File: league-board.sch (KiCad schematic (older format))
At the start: 14 parts

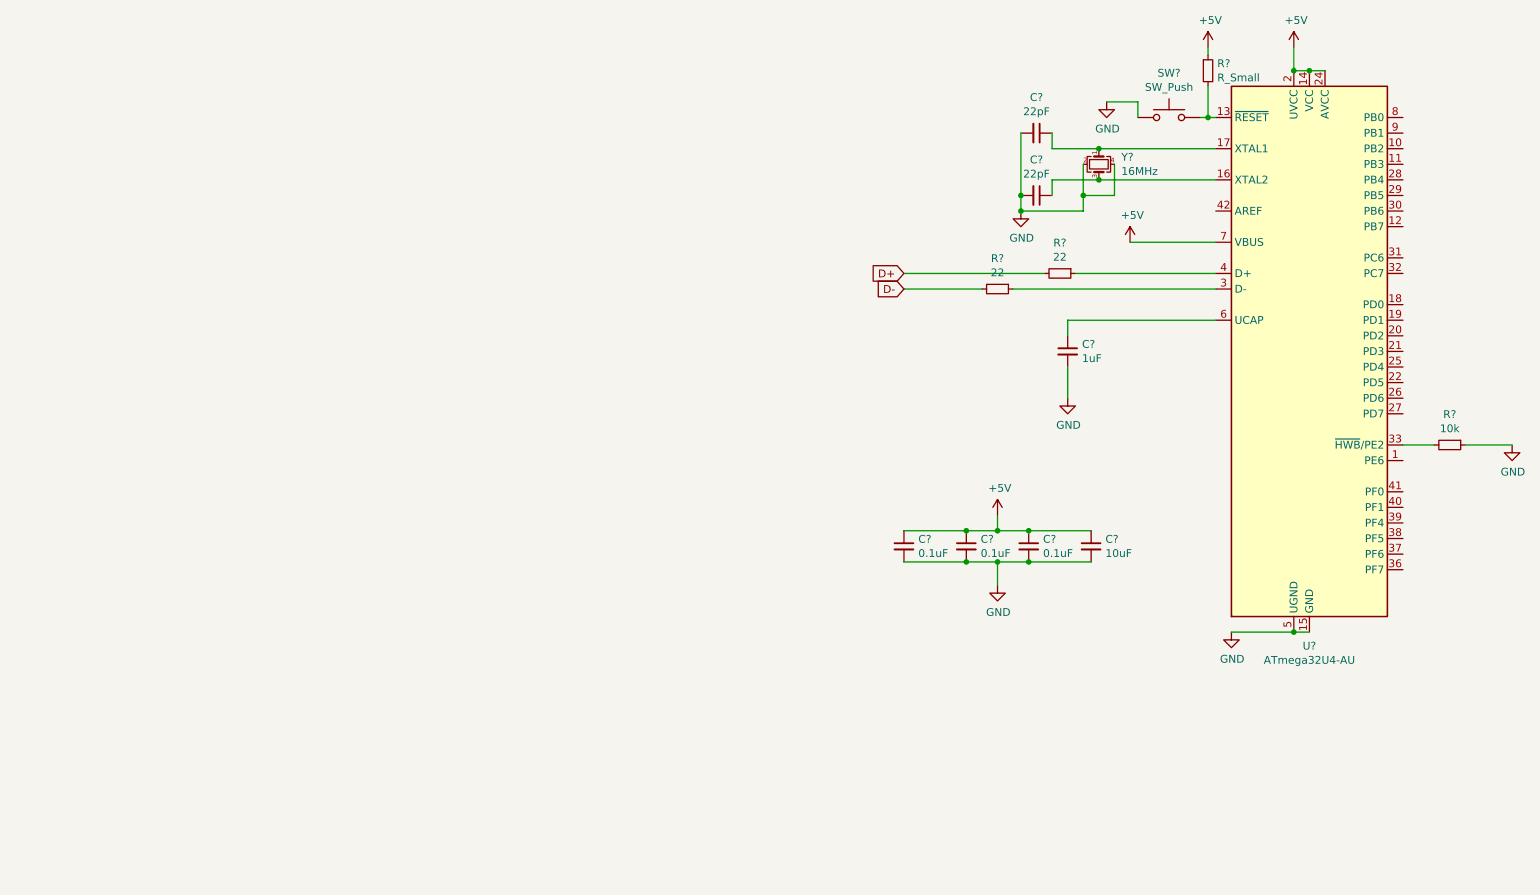
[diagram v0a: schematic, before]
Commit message: usb + switch slots added to schematic
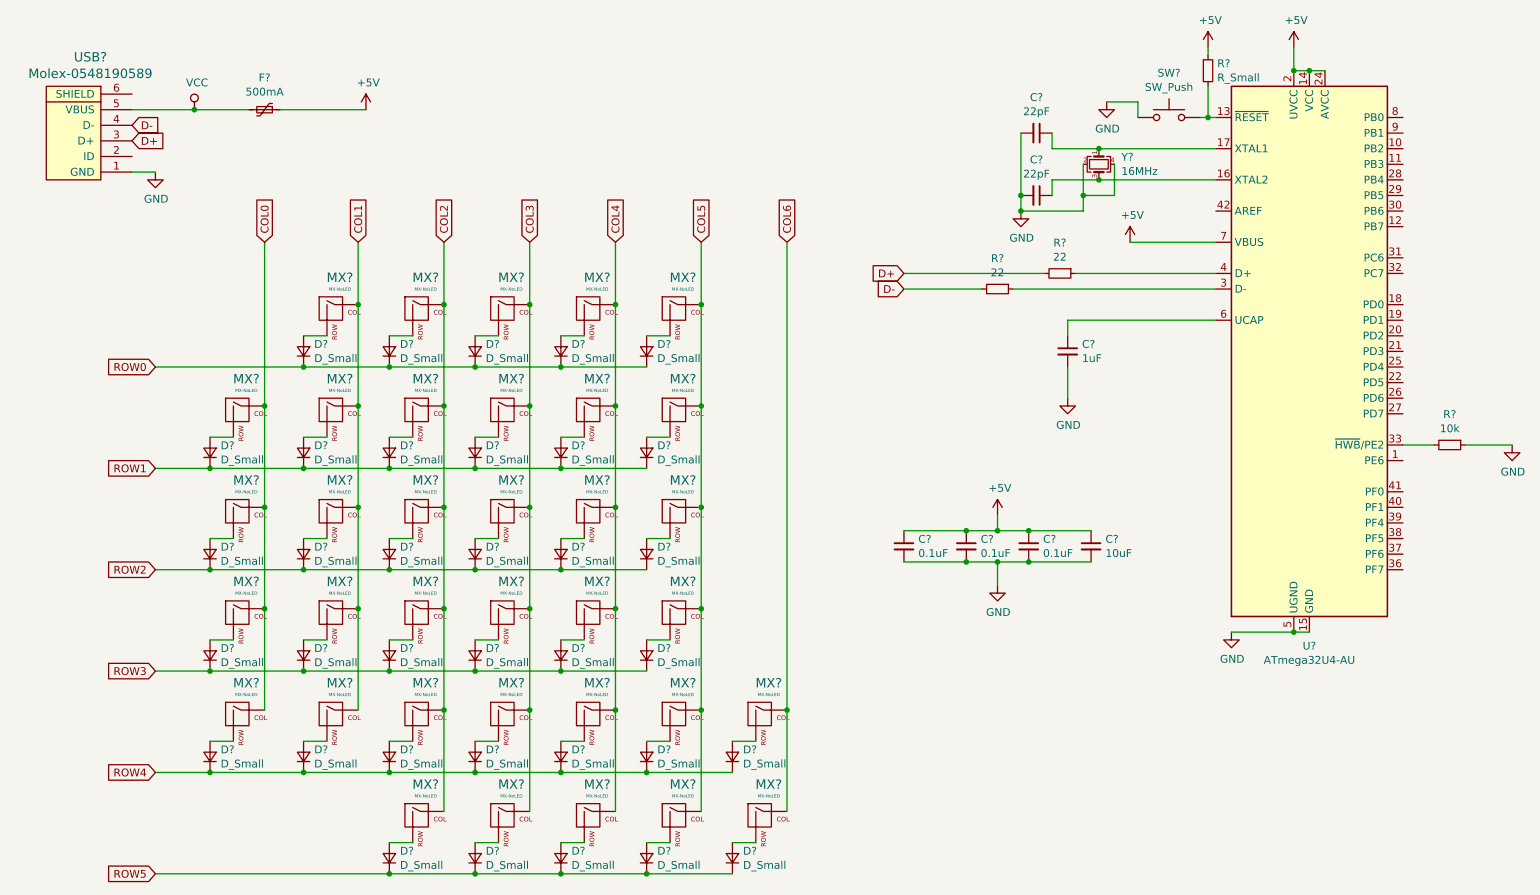
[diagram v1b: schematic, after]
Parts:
- added D? (x35): D_Small, symbol Device:D_Small
- added F?: 500mA, symbol Device:Polyfuse_Small
- added MX? (x35): MX-NoLED, symbol MX_Alps_Hybrid:MX-NoLED
- added USB?: Molex-0548190589, symbol random-keyboard-parts:Molex-0548190589
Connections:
- net +5V: now also F?.1
- net D+: now also USB?.3 (D+)
- net D-: now also USB?.4 (D-)
- net GND: now also USB?.1 (GND)
- new net: D?.2 (A), MX?.2 (ROW) (x35)
- new net COL0: MX?.1 (COL), MX?.1 (COL), MX?.1 (COL), MX?.1 (COL)
- new net COL1: MX?.1 (COL), MX?.1 (COL), MX?.1 (COL), MX?.1 (COL), MX?.1 (COL)
- new net COL2: MX?.1 (COL), MX?.1 (COL), MX?.1 (COL), MX?.1 (COL), MX?.1 (COL), MX?.1 (COL)
- new net COL3: MX?.1 (COL), MX?.1 (COL), MX?.1 (COL), MX?.1 (COL), MX?.1 (COL), MX?.1 (COL)
- new net COL4: MX?.1 (COL), MX?.1 (COL), MX?.1 (COL), MX?.1 (COL), MX?.1 (COL), MX?.1 (COL)
- new net COL5: MX?.1 (COL), MX?.1 (COL), MX?.1 (COL), MX?.1 (COL), MX?.1 (COL), MX?.1 (COL)
- new net COL6: MX?.1 (COL), MX?.1 (COL)
- new net ROW0: D?.1 (K), D?.1 (K), D?.1 (K), D?.1 (K), D?.1 (K)
- new net ROW1: D?.1 (K), D?.1 (K), D?.1 (K), D?.1 (K), D?.1 (K), D?.1 (K)
- new net ROW2: D?.1 (K), D?.1 (K), D?.1 (K), D?.1 (K), D?.1 (K), D?.1 (K)
- new net ROW3: D?.1 (K), D?.1 (K), D?.1 (K), D?.1 (K), D?.1 (K), D?.1 (K)
- new net ROW4: D?.1 (K), D?.1 (K), D?.1 (K), D?.1 (K), D?.1 (K), D?.1 (K), D?.1 (K)
- new net ROW5: D?.1 (K), D?.1 (K), D?.1 (K), D?.1 (K), D?.1 (K)
- new net VCC: F?.2, USB?.5 (VBUS)

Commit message: finished schematic, may need to fiddle with switch placment
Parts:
- C1, C2, C3, C4, C5, C6, C7: renamed from C?; footprint (none) -> Capacitor_SMD:C_0805_2012Metric
- D1, D10, D11, D12, D13, D14, D15, D16, D17, D18, D19, D2, D20, D21, D22, D23, D24, D25, D26, D27, D28, D29, D3, D30, D31, D32, D33, D34, D35, D4, D5, D6, D7, D8, D9: renamed from D?; footprint (none) -> Diode_SMD:D_SOD-123
- F1: renamed from F?; footprint (none) -> Fuse:Fuse_1206_3216Metric
- MX1, MX10, MX11, MX12, MX13, MX14, MX15, MX16, MX17, MX18, MX19, MX2, MX20, MX21, MX22, MX23, MX24, MX25, MX26, MX27, MX28, MX29, MX3, MX30, MX31, MX32, MX33, MX34, MX4, MX5, MX6, MX7, MX8, MX9: renamed from MX?; footprint (none) -> MX_Alps_Hybrid:MX-1U-NoLED
- MX35: renamed from MX?; footprint (none) -> MX_Alps_Hybrid:MX-2U-NoLED
- R1, R2, R4: renamed from R?; footprint (none) -> Resistor_SMD:R_0805_2012Metric
- R3: renamed from R?; value R_Small -> 10k; footprint (none) -> Resistor_SMD:R_0805_2012Metric
- SW1: renamed from SW?; footprint (none) -> random-keyboard-parts:SKQG-1155865
- USB1: renamed from USB?; footprint (none) -> random-keyboard-parts:Molex-0548190589
- Y1: renamed from Y?; footprint (none) -> Crystal:Crystal_SMD_3225-4Pin_3.2x2.5mm
- gave numbers to parts that had none: 1
